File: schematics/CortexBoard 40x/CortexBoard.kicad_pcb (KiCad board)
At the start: 2 copper layers, 30 parts, among them J1 Cortex Serial CLI, J2 UART6 Connector, J3 Odroid Power, J4 Switches, J5 LevelShifter_in, J6 LevelShifter-Out, J7 Cortex I2C CLI, J8 Cortex-Power-In, J9 Power-Out, P1 Battery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

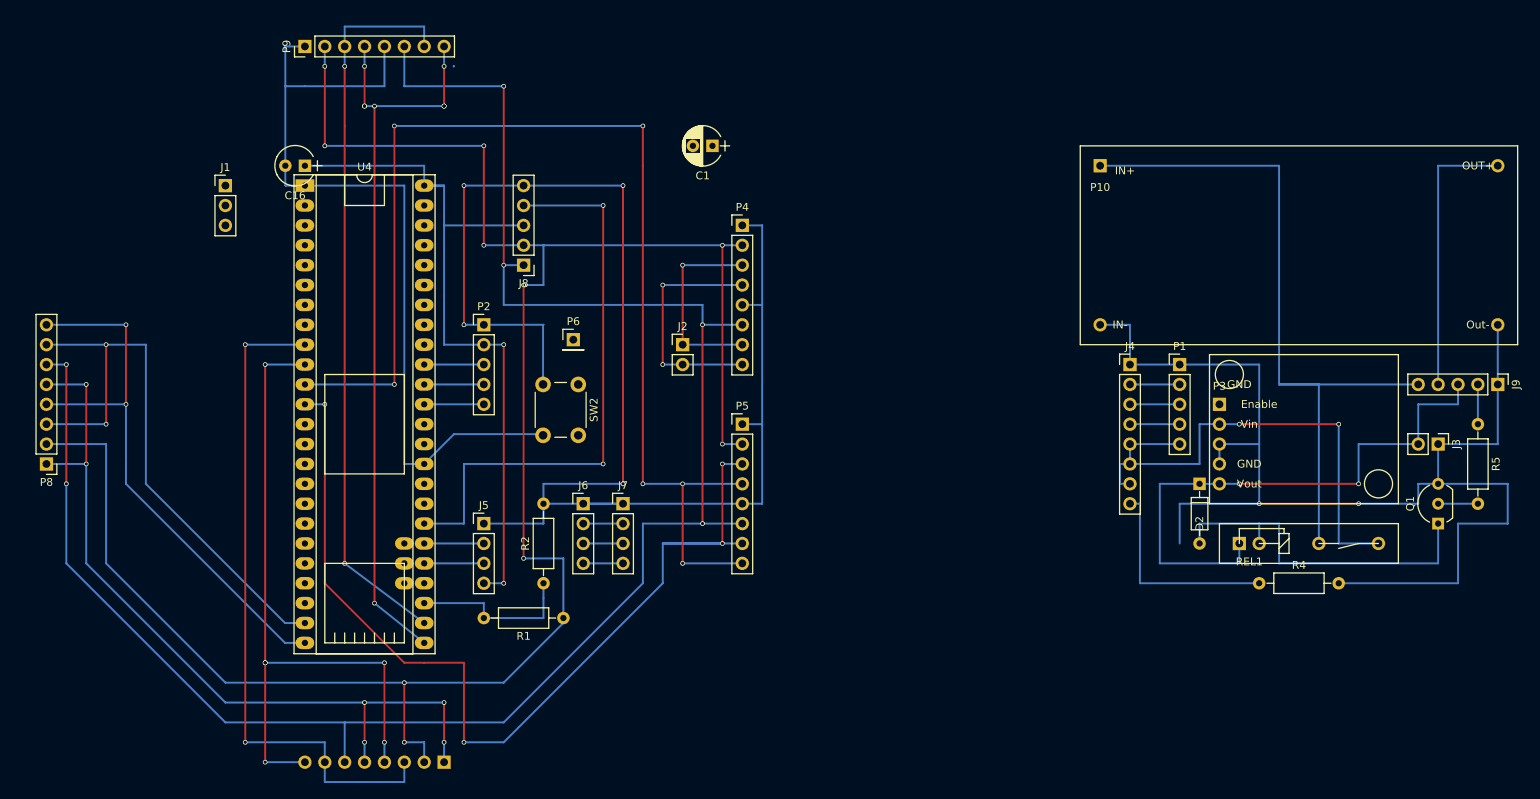
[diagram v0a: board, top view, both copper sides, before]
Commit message: added cad
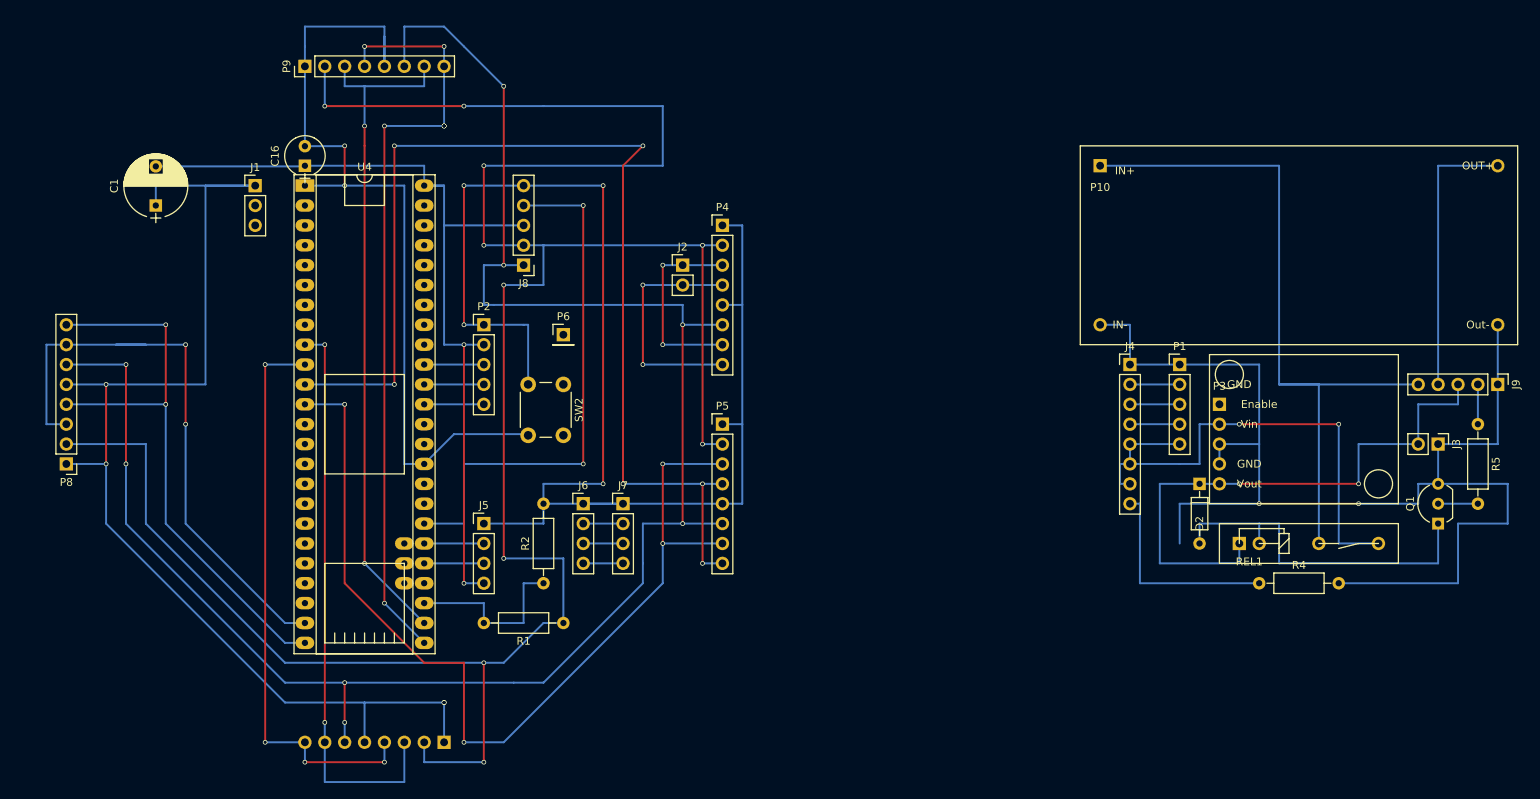
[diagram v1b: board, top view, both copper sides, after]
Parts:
- C1: footprint Capacitors_THT:CP_Radial_D5.0mm_P2.50mm -> Capacitors_THT:CP_Radial_D8.0mm_P5.00mm
- moved C1 71.5 mm to (73.7, 74.9), turned to 90 degrees
- moved J2 10.2 mm to (141.0, 82.5)
- moved J1 3.81 mm to (86.4, 72.4)
- moved P7 2.54 mm to (110.5, 143.5)
- moved P8 2.54 mm to (62.2, 108.0)
- moved P9 2.54 mm to (92.7, 57.1)
- moved P4 2.54 mm to (146.1, 77.5)
- moved P5 2.54 mm to (146.1, 102.9)
- moved SW2 1.91 mm to (125.7, 97.8)
- moved P6 1.42 mm to (125.7, 91.4)
- moved R1 0.64 mm to (125.7, 128.3)
- turned C16 to 90 degrees
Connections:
- net /VDD_10V renamed /Vout+10V
- net /VIn+10V renamed /+10V
- net /VIn+14V renamed /+14V
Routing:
- net /+10V: track 266.0 -> 315.5 mm
- net /GND: track 402.7 -> 444.2 mm
- net /VIn+5V: track 94.0 -> 110.5 mm
- net /RX3: track 88.9 -> 73.7 mm, vias 6 -> 4
- net /TX3: track 86.4 -> 73.7 mm
- net /RX2: track 152.4 -> 143.3 mm
- net /TX5: track 94.0 -> 87.0 mm
- net /TX4: track 76.3 -> 81.8 mm
- net /TX2: track 126.9 -> 121.8 mm
- net /Relay-Out: track 73.7 -> 68.6 mm
- net /+14V: track 249.5 -> 245.4 mm, vias 6 -> 8
- net /RX4: track 72.6 -> 75.5 mm
- net /RX5: track 97.0 -> 98.6 mm, vias 8 -> 6
- net Net-(R1-Pad2): track 21.6 -> 22.9 mm

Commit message: layout improvements
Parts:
- removed J5: LevelShifter_in, Pin_Headers:Pin_Header_Straight_1x04_Pitch2.54mm
- removed J6: LevelShifter-Out, Pin_Headers:Pin_Header_Straight_1x04_Pitch2.54mm
- added U1: I2C_LevelShifter, Cortex:I2C_LevelShifter, F.Cu at (115.6, 113.0)
- moved Q1 68.3 mm to (190.5, 66.0), turned to 180 degrees
- moved REL1 54.6 mm to (195.6, 66.0)
- moved D2 49.6 mm to (195.6, 62.2), turned to 0 degrees
- moved R4 27.1 mm to (188.0, 118.1)
- moved P1 26.8 mm to (177.8, 97.8)
- moved R5 20.1 mm to (223.5, 96.5), turned to 180 degrees
- moved J3 19.2 mm to (218.4, 108.0)
- moved P3 19.2 mm to (190.5, 102.9)
- moved J9 19.2 mm to (226.1, 100.3)
- moved P10 19.2 mm to (175.3, 77.5)
- moved P6 16.0 mm to (123.8, 107.3)
- moved J4 13.0 mm to (185.4, 97.8)
- moved P2 8.64 mm to (123.8, 87.6)
- moved C1 8.13 mm to (80.0, 69.8), turned to 180 degrees
- moved SW2 6.54 mm to (120.0, 101.0)
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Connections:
- net /Switch2 renamed /Switch2/LEDAnode
- R1 pad 1: /+10V -> /+14V
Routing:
- net Net-(Q1-Pad2): track 5.08 -> 76.8 mm
- net /+10V: track 315.5 -> 258.0 mm, vias 10 -> 8
- net /+5V: track 73.7 -> 125.3 mm, vias 2 -> 0
- net Net-(D2-Pad2): track 45.7 -> 19.0 mm
- net /Switch2/LEDAnode: track 57.2 -> 80.1 mm, vias 2 -> 3
- net /LEDKathode: track 26.7 -> 5.08 mm
- net /TX2: track 121.8 -> 104.9 mm
- net /Vout+14V: track 94.0 -> 77.5 mm
- net /VIn+5V: track 110.5 -> 124.6 mm
- net /TX4: track 81.8 -> 70.4 mm
- net /GND: track 444.2 -> 434.0 mm, vias 10 -> 8
- net /SDA: track 7.62 -> 15.9 mm
- net /SCL: track 7.62 -> 15.9 mm
- net /RST: track 7.62 -> 15.9 mm
- net /Relay-Out: track 68.6 -> 62.9 mm
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
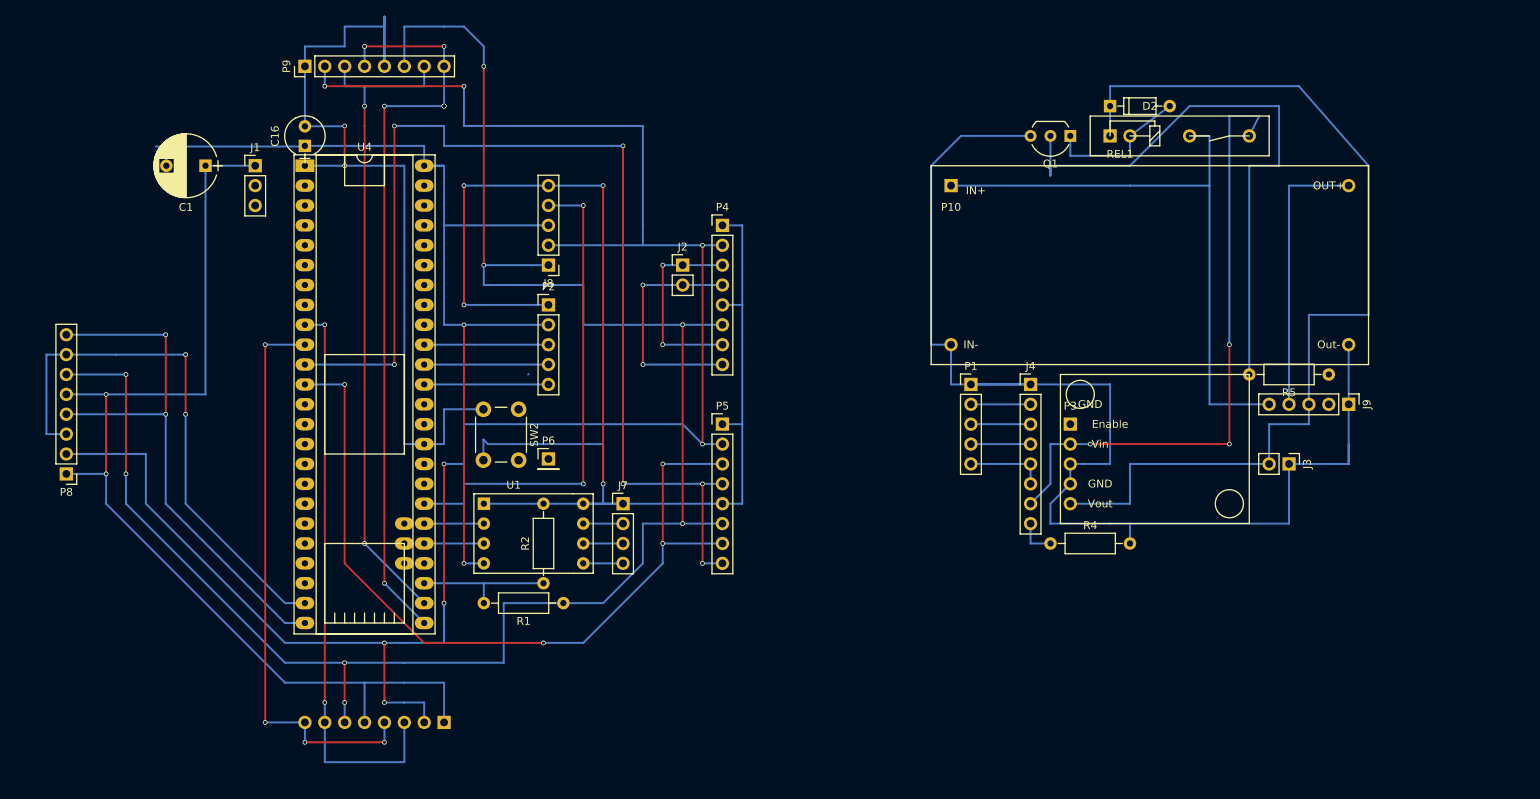
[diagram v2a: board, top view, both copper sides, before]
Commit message: made new power supply board
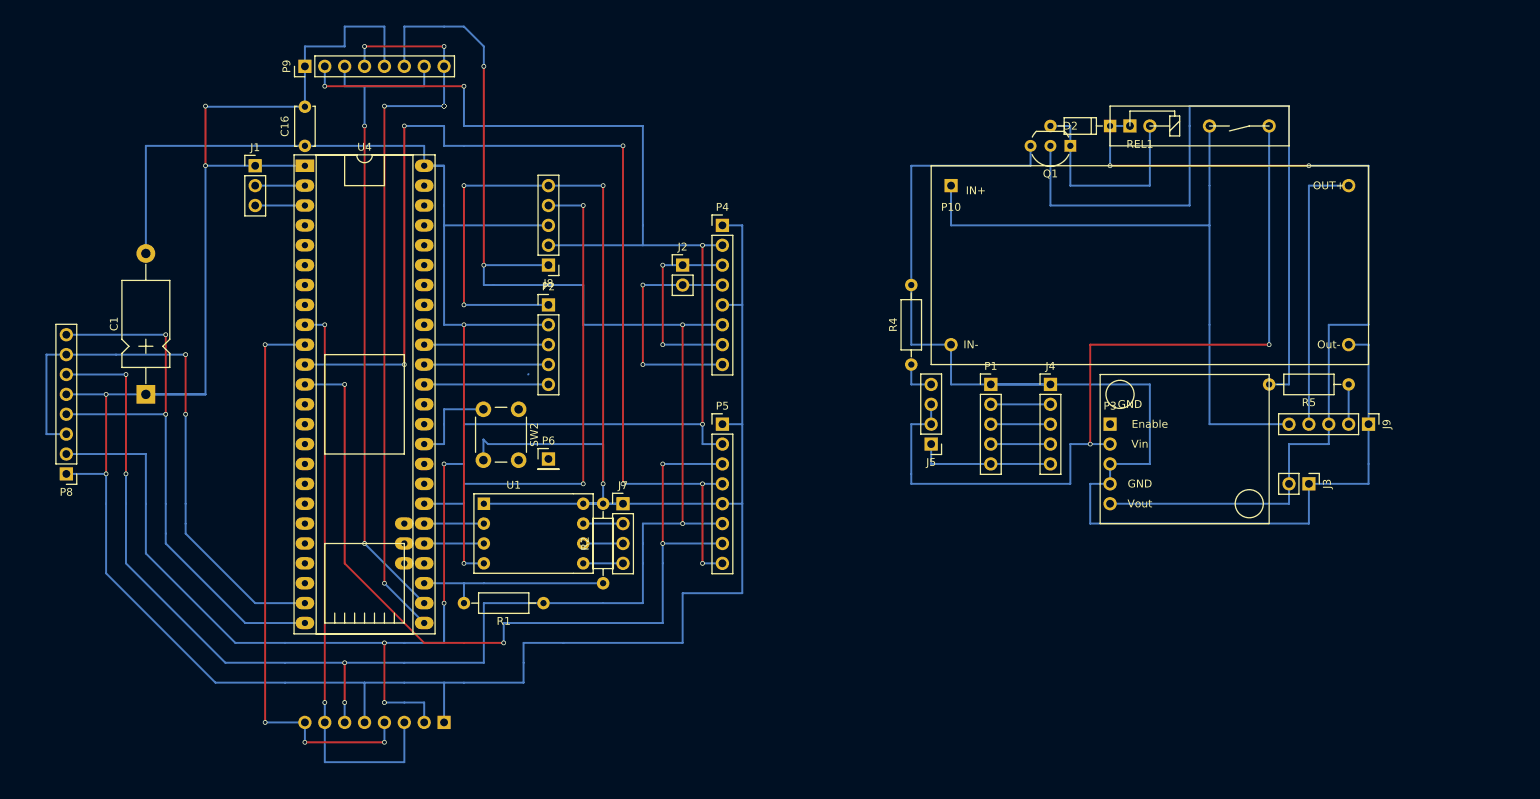
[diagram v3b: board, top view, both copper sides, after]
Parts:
- added J5: LED/Switch, Pin_Headers:Pin_Header_Straight_1x04_Pitch2.54mm, F.Cu at (172.7, 105.4)
- C1: footprint Capacitors_THT:CP_Radial_D8.0mm_P5.00mm -> Capacitors_THT:CP_Axial_L11.0mm_D6.0mm_P18.00mm_Horizontal
- C16: footprint Capacitors_THT:CP_Radial_Tantal_D5.0mm_P2.50mm -> Capacitors_THT:C_Disc_D5.0mm_W2.5mm_P5.00mm
- J4: footprint Pin_Headers:Pin_Header_Straight_1x08_Pitch2.54mm -> Pin_Headers:Pin_Header_Straight_1x05_Pitch2.54mm
- moved C1 30.2 mm to (72.4, 99.1), turned to 90 degrees
- moved R4 29.0 mm to (170.2, 95.2), turned to 90 degrees
- moved R2 7.62 mm to (130.8, 123.2)
- moved P3 5.08 mm to (195.6, 102.9)
- moved J9 3.59 mm to (228.6, 102.9)
- moved J3 3.59 mm to (221.0, 110.5)
- moved R5 2.84 mm to (226.1, 97.8)
- moved REL1 2.84 mm to (198.1, 64.8)
- moved J4 2.54 mm to (188.0, 97.8)
- moved R1 2.54 mm to (123.2, 125.7)
- moved D2 2.54 mm to (195.6, 64.8), turned to 180 degrees
- moved P1 2.54 mm to (180.3, 97.8)
- moved Q1 1.27 mm to (190.5, 67.3)
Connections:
- P3 pad 2: /Switch2/LEDAnode -> /Switch2/Vin
- REL1 pad 4: /Switch2/LEDAnode -> /Switch2/Vin
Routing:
- net /Switch2/Vin: track 0.00 -> 106.7 mm, vias 0 -> 3
- net /Switch2/LEDAnode: track 80.1 -> 0.00 mm, vias 3 -> 0
- net /GND: track 434.0 -> 467.2 mm
- net /VIn+5V: track 124.6 -> 137.1 mm
- net Net-(Q1-Pad2): track 76.8 -> 88.9 mm
- net Net-(D2-Pad2): track 19.0 -> 27.9 mm
- net /Vout+14V: track 77.5 -> 86.4 mm
- net /+5V: track 125.3 -> 116.8 mm, vias 0 -> 2
- net /Batt+: track 10.2 -> 17.8 mm
- net Net-(R1-Pad2): track 17.8 -> 25.4 mm
- net /Batt-: track 162.7 -> 170.2 mm
- net /+14V: track 248.4 -> 255.9 mm
- net /TX: track 0.00 -> 6.35 mm
- net /RX: track 0.00 -> 6.35 mm
- net /TX2: track 104.9 -> 110.9 mm
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
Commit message: new Elko to stabilize servo voltage
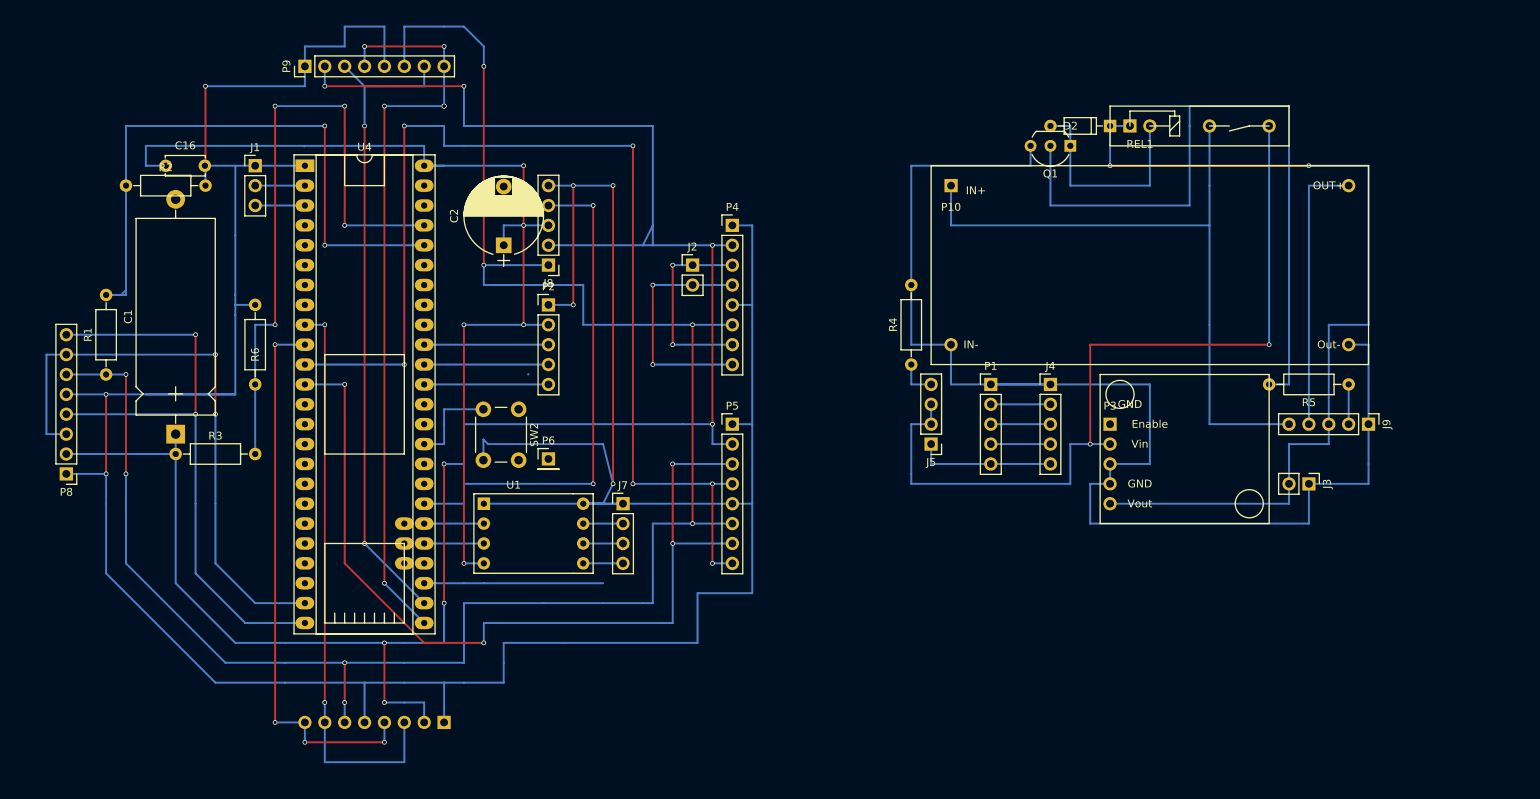
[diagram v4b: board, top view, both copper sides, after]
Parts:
- added C2: 220uF, Capacitors_THT:CP_Radial_D10.0mm_P7.50mm, F.Cu at (118.1, 80.0)
- added R3: 150K, Resistors_THT:R_Axial_DIN0207_L6.3mm_D2.5mm_P10.16mm_Horizontal, F.Cu at (76.2, 106.7)
- added R6: 10K, Resistors_THT:R_Axial_DIN0207_L6.3mm_D2.5mm_P10.16mm_Horizontal, F.Cu at (86.4, 97.8)
- C1: value 470uF -> 4700uF; footprint Capacitors_THT:CP_Axial_L11.0mm_D6.0mm_P18.00mm_Horizontal -> Capacitors_THT:CP_Axial_L25.0mm_D10.0mm_P30.00mm_Horizontal
- R1: value 82K -> 150K
- moved R2 79.4 mm to (69.8, 72.4), turned to 0 degrees
- moved R1 63.1 mm to (67.3, 96.5), turned to 90 degrees
- moved C16 18.0 mm to (74.9, 69.8), turned to 0 degrees
- moved C1 6.35 mm to (76.2, 104.1)
- moved J2 1.27 mm to (142.2, 82.5)
- moved P4 1.27 mm to (147.3, 77.5)
- moved P5 1.27 mm to (147.3, 102.9)
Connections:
- C1 pad 1: /GND -> /+10V
- C1 pad 2: /VIn+5V -> /GND
- U4 pad 27: Net-(R1-Pad2) -> (no net)
- U4 pad 44: (no net) -> Net-(R1-Pad2)
- U4 pad 45: (no net) -> Net-(R3-Pad2)
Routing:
- net Net-(R3-Pad2): track 0.00 -> 81.3 mm, vias 0 -> 4
- net Net-(R1-Pad2): track 25.4 -> 93.6 mm, vias 0 -> 2
- net (no net): track 0.08 -> 22.9 mm
- net /+10V: track 260.6 -> 271.8 mm
- net /VIn+5V: track 137.1 -> 130.9 mm, vias 2 -> 5
- net /RX4: track 74.7 -> 80.7 mm
- net /RX3: track 73.7 -> 71.1 mm
- net /Relay-Out: track 62.9 -> 65.4 mm
- net /TX4: track 72.6 -> 74.8 mm
- net /GND: track 467.2 -> 465.7 mm
- net /TX5: track 84.4 -> 82.9 mm
- net /+14V: track 255.9 -> 257.1 mm
- net /TX2: track 110.9 -> 112.2 mm
- net /RX2: track 142.2 -> 143.5 mm

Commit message: layout
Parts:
- C16: footprint Capacitors_THT:C_Disc_D5.0mm_W2.5mm_P5.00mm -> Capacitors_THT:C_Rect_L7.0mm_W2.5mm_P5.00mm
- C2: footprint Capacitors_THT:CP_Radial_D10.0mm_P7.50mm -> Capacitors_THT:CP_Radial_D8.0mm_P5.00mm
- J4: value Switches -> Bodysocket
- J5: footprint Pin_Headers:Pin_Header_Straight_1x04_Pitch2.54mm -> Pin_Headers:Pin_Header_Straight_1x05_Pitch2.54mm
- J9: value Power-Out -> Cortex-Power-Out
- moved P1 7.62 mm to (188.0, 97.8)
- moved J4 6.35 mm to (181.6, 97.8)
- moved C2 3.59 mm to (115.6, 77.5)
- moved J5 3.59 mm to (175.3, 108.0)
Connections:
- J5 pad 1: /Batt+ -> /SW2/Batt
- J5 pad 2: /Switch2/Vin -> /Batt+
- J5 pad 3: /Switch2/Vin -> /LEDAnode
- J5 pad 4: /LEDKathode -> /LEDAnode
- P1 pad 5: /Batt+ -> /SW2/Batt
- P3 pad 2: /Switch2/Vin -> (no net)
- REL1 pad 4: /Switch2/Vin -> /LEDAnode
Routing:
- net /LEDAnode: track 0.00 -> 111.8 mm, vias 0 -> 3
- net /Switch2/Vin: track 106.7 -> 0.00 mm, vias 3 -> 0
- net /SW2/Batt: track 0.00 -> 17.8 mm
- net /+14V: track 257.1 -> 266.2 mm
- net /Batt+: track 17.8 -> 8.89 mm
- net /GND: track 465.7 -> 474.1 mm
- net /+10V: track 271.8 -> 269.0 mm
- net /LEDKathode: track 5.08 -> 7.62 mm
- net /Batt-: track 170.2 -> 171.4 mm

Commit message: a weekend's work
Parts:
- removed J1: Cortex Serial CLI, Pin_Headers:Pin_Header_Straight_1x03_Pitch2.54mm
- C1: value 4700uF -> 2200uF
- J5: footprint Pin_Headers:Pin_Header_Straight_1x05_Pitch2.54mm -> Pin_Headers:Pin_Header_Straight_1x04_Pitch2.54mm
- J7: value Cortex I2C CLI -> CORTEX CLI; footprint Pin_Headers:Pin_Header_Straight_1x04_Pitch2.54mm -> Pin_Headers:Pin_Header_Straight_1x06_Pitch2.54mm
- P2: footprint Pin_Headers:Pin_Header_Straight_1x05_Pitch2.54mm -> Pin_Headers:Pin_Header_Straight_1x06_Pitch2.54mm
- moved R4 47.2 mm to (213.4, 114.3)
- moved C16 38.1 mm to (113.0, 69.8)
- moved J5 25.0 mm to (196.8, 120.7), turned to 90 degrees
- moved J9 14.2 mm to (215.9, 96.5), turned to 90 degrees
- moved J7 13.0 mm to (130.8, 125.7), turned to 180 degrees
- moved P3 10.9 mm to (204.5, 96.5), turned to 270 degrees
- moved P1 10.9 mm to (177.8, 101.6), turned to 90 degrees
- moved J3 10.2 mm to (215.9, 101.6), turned to 90 degrees
- moved J2 9.25 mm to (133.3, 80.0)
- moved R5 8.13 mm to (231.1, 91.4), turned to 90 degrees
- moved P2 6.25 mm to (118.1, 85.1)
- moved Q1 5.24 mm to (185.4, 66.0)
- moved J4 4.02 mm to (177.8, 96.5), turned to 90 degrees
- moved R3 4.02 mm to (72.4, 108.0)
- moved J8 3.17 mm to (125.7, 80.0)
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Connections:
- J5 pad 3: /LEDAnode -> /SW1/VIN/LEDAnode
- J5 pad 4: /LEDAnode -> /LEDKathode
- J7 pad 1: /GND -> Net-(J7-Pad1)
- J7 pad 2: /SDA-ODroid -> /RX
- J7 pad 3: /SCL-ODroid -> /3.3V_ODroid
- J7 pad 4: /3.3V_ODroid -> /SCL-ODroid
- J9 pad 1: /Batt- -> /Vout+14V
- J9 pad 2: Net-(J9-Pad2) -> /Vout+10V
- J9 pad 4: /Vout+10V -> Net-(J9-Pad4)
- J9 pad 5: /Vout+14V -> /Batt-
- P2 pad 1: /GND -> /VIn+5V
- P2 pad 2: /VIn+5V -> (no net)
- P2 pad 3: /SDA -> /GND
- P2 pad 4: /SCL -> /SDA
- P2 pad 5: /RST -> /SCL
- P3 pad 2: (no net) -> /SW1/VIN/LEDAnode
- R5 pad 1: Net-(J9-Pad2) -> Net-(J9-Pad4)
- REL1 pad 4: /LEDAnode -> /SW1/VIN/LEDAnode
- U4 pad 3: /TX -> Net-(J7-Pad1)
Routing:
- net /LEDAnode: track 111.8 -> 0.00 mm, vias 3 -> 0
- net /SW1/VIN/LEDAnode: track 0.00 -> 71.1 mm, vias 0 -> 2
- net /VIn+5V: track 130.9 -> 66.0 mm, vias 5 -> 2
- net /Batt-: track 171.4 -> 116.8 mm, vias 0 -> 4
- net /Batt+: track 8.89 -> 35.6 mm
- net /+5V: track 116.8 -> 91.4 mm, vias 2 -> 4
- net (no net): track 22.9 -> 0.11 mm, vias 0 -> 1
- net Net-(J9-Pad4): track 0.00 -> 17.8 mm
- net /GND: track 474.1 -> 488.0 mm, vias 8 -> 6
- net /RX4: track 80.7 -> 91.1 mm
- net /Vout+14V: track 86.4 -> 76.2 mm
- net /SW2/Batt: track 17.8 -> 27.9 mm
- net /+14V: track 266.2 -> 276.3 mm
- net Net-(R1-Pad2): track 93.6 -> 103.5 mm
- net /TX4: track 74.8 -> 84.7 mm
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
